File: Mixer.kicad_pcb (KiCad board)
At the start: 2 copper layers, 123.1 x 128.5 mm, 52 parts, among them J1 Eurorack 2x8hs, J13 OUT1, J17 IN1, J18 IN2, J19 IN3, J20 IN4, J21 IN5, U1 TL072, U2 LM3915N

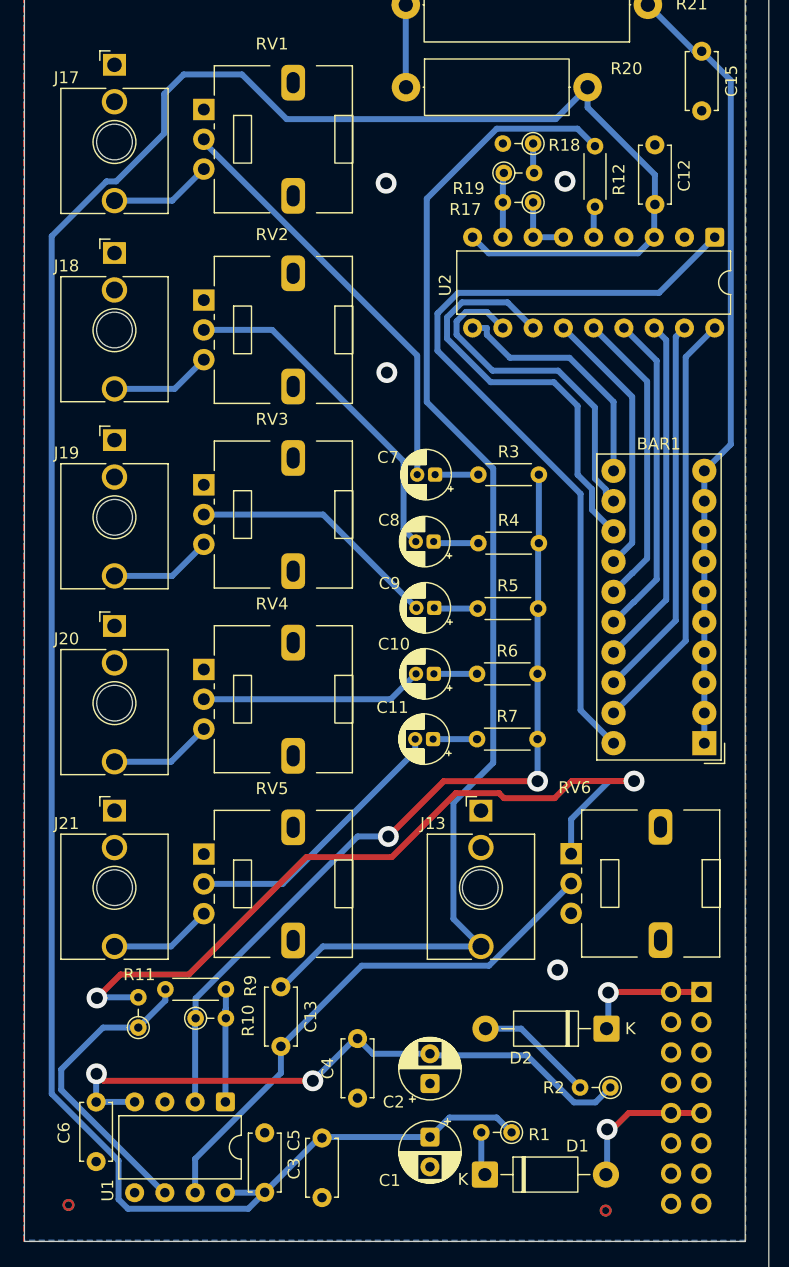
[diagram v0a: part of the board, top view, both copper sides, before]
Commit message: spaced PCB routing
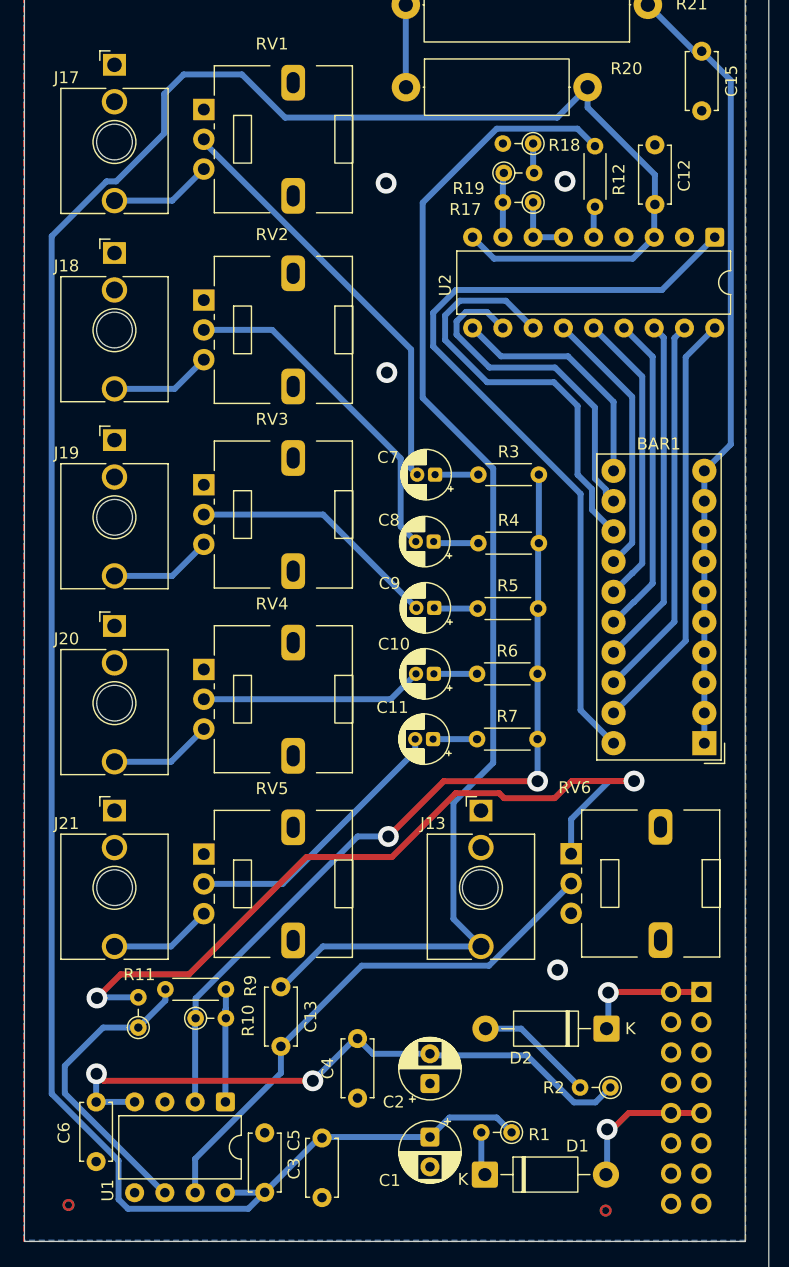
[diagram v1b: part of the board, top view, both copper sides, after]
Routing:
- net Net-(BAR1H-K): track 35.5 -> 36.1 mm
- net Net-(BAR1A-K): track 68.1 -> 68.7 mm

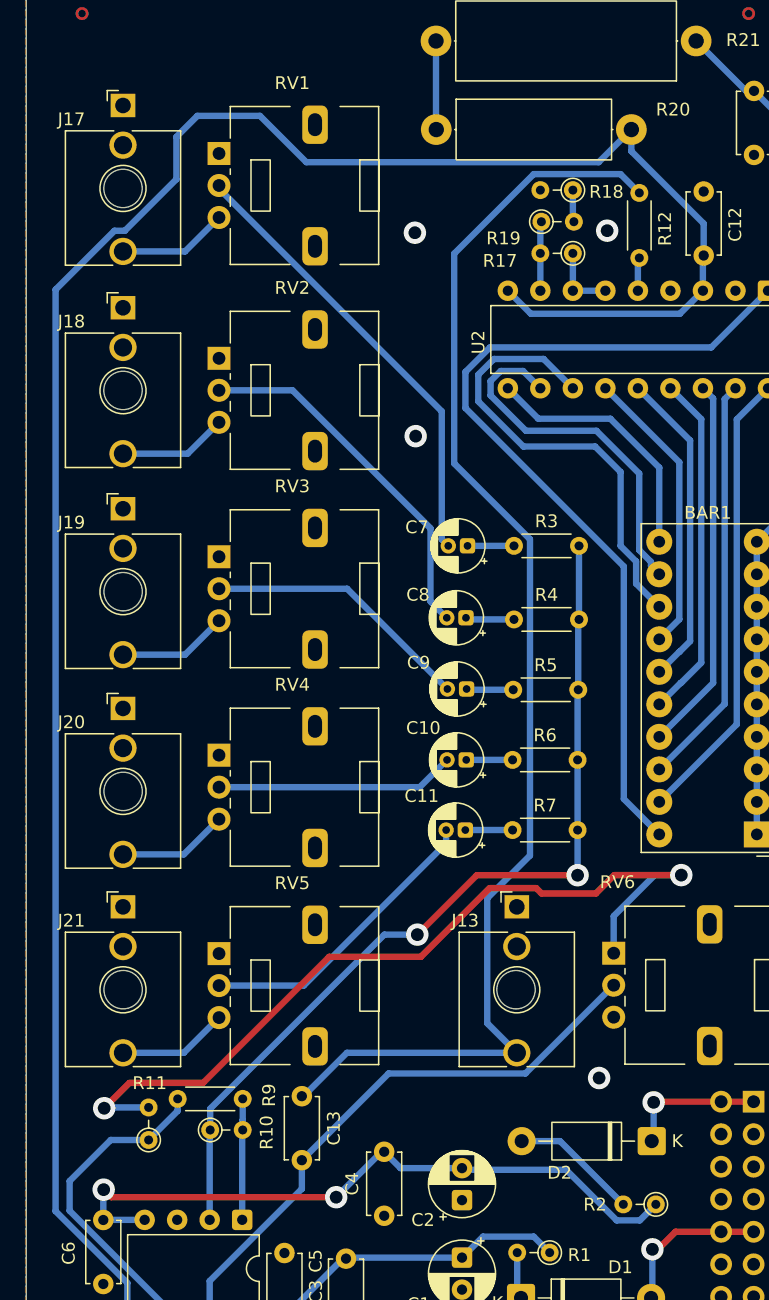
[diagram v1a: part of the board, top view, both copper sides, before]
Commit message: Update to reduce FP traces and final self-etch print.
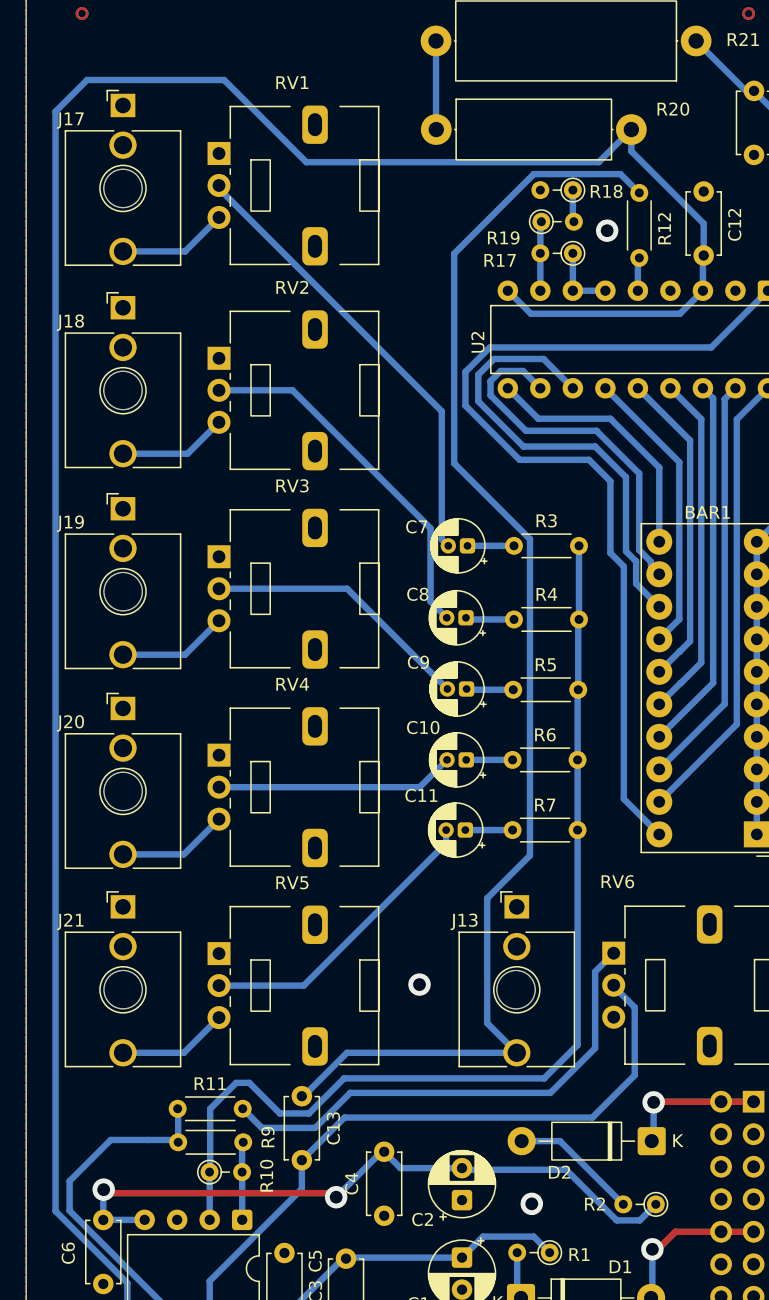
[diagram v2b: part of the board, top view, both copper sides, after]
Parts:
- R11: footprint Resistor_THT:R_Axial_DIN0204_L3.6mm_D1.6mm_P2.54mm_Vertical -> Resistor_THT:R_Axial_DIN0204_L3.6mm_D1.6mm_P5.08mm_Horizontal
- moved R10 3.39 mm to (44.0, 123.2)
- moved R11 3.33 mm to (38.9, 120.6), turned to 0 degrees
- moved R9 3.29 mm to (41.4, 125.5)
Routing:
- net Net-(R11-Pad2): track 66.0 -> 38.8 mm, vias 2 -> 0
- net Net-(U1A--): track 71.0 -> 80.5 mm, vias 2 -> 0
- net +12v: track 210.3 -> 218.9 mm
- net Net-(C13-Pad2): track 45.3 -> 51.7 mm
- net Net-(R10-Pad1): track 9.50 -> 6.10 mm
- net Net-(BAR1A-K): track 68.7 -> 71.8 mm
- net Net-(U1B--): track 25.8 -> 26.7 mm
- net GND: vias 4 -> 3
